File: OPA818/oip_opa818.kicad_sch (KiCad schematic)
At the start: 32 parts, among them J101 Conn_Coaxial, J102 Conn_01x03, U101 LT3042xMSE, U102 LT3093xMSE, U103 OPA818IDRGx, U104 BUF602xDBV

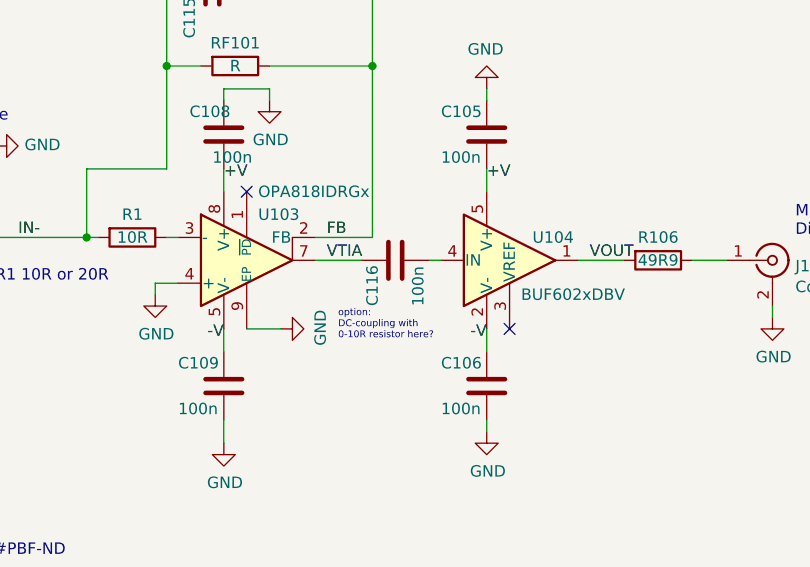
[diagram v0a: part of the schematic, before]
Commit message: dc-coupling for BUF602
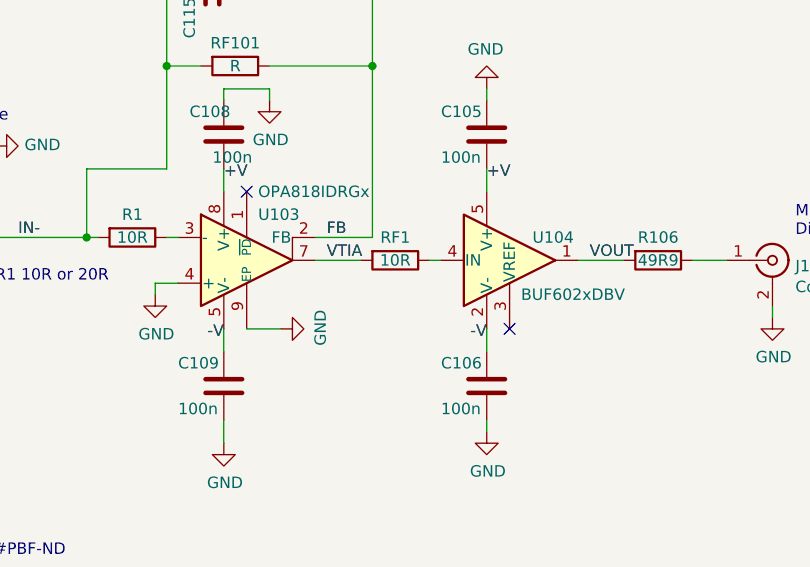
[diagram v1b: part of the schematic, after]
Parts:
- removed C116: 100n, Capacitor_SMD:C_0402_1005Metric, symbol Device:C
- added RF1: 10R, Resistor_SMD:R_0402_1005Metric, symbol Device:R
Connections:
- net VTIA: now also RF1.2
- net at U104.4 (IN): now also RF1.1
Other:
- note removed: "option: DC-coupling with 0-10R resistor here?"
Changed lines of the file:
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@@
     (effects (font (size 1.27 1.27)) (justify left bottom))
-  )
-  (text "option:\nDC-coupling with \n0-10R resistor here?" (at 129.54 86.36 0)
-    (effects (font (size 0.762 0.762)) (justify left bottom))
   )
   (text "SOD323F" (at 48.26 124.46 0)
@@
     (pin "1")
   )
-  (symbol (lib_id "Device:C") (at 135.89 77.47 90) (unit 1)
-    (in_bom yes) (on_board yes)
-    (property "Reference" "C116" (id 0) (at 133.35 82.55 0)
-      (effects (font (size 1.27 1.27)) (justify left))
-    )
-    (property "Value" "100n" (id 1) (at 138.43 82.55 0)
-      (effects (font (size 1.27 1.27)) (justify left))
-    )
-    (property "Footprint" "Capacitor_SMD:C_0402_1005Metric" (id 2) (at 139.7 76.5048 0)
+  (symbol (lib_id "Device:R") (at 135.89 77.47 270) (unit 1)
+    (in_bom yes) (on_board yes)
+    (property "Reference" "RF1" (id 0) (at 135.89 74.93 90))
+    (property "Value" "10R" (id 1) (at 135.89 77.47 90))
+    (property "Footprint" "Resistor_SMD:R_0402_1005Metric" (id 2) (at 135.89 75.692 90)
       (effects (font (size 1.27 1.27)) hide)
     )
@@
       (reference "C115") (unit 1) (value "C") (footprint "Capacitor_SMD:C_0402_1005Metric")
     )
-    (path "/00000000-0000-0000-0000-00005f175d9c"
-      (reference "C116") (unit 1) (value "100n") (footprint "Capacitor_SMD:C_0402_1005Metric")
-    )
     (path "/00000000-0000-0000-0000-00005dfdaa2e"
       (reference "D101") (unit 1) (value "D") (footprint "Diode_SMD:D_SOD-323F")
@@
       (reference "R107") (unit 1) (value "56k") (footprint "Resistor_SMD:R_0603_1608Metric")
     )
+    (path "/df83dace-7d40-4784-a916-9861fd8c1302"
+      (reference "RF1") (unit 1) (value "10R") (footprint "Resistor_SMD:R_0402_1005Metric")
+    )
     (path "/00000000-0000-0000-0000-00005e082b6c"
